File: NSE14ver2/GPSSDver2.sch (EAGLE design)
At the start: 30 parts, among them CN1 DM3AT, Q2 16mhz

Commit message: 修正
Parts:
- removed LED4, LED6: (no value), led:LED5MM
- added L1, L2: (no value), Chip LED:OSXX1608C1A
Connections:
- removed net N$12: C3.1, R16.2, SW1.P$2, U$3.PC6RESET
- new net RESETB: C3.1, JP1.6, R16.2, SW1.P$2, U$3.PC6RESET
- net +5V: now also R16.1
- net GND: now also L1.CT, L2.CT; no longer LED4.C, LED6.C, R16.1
- net N$1: now also L2.AN; no longer LED6.A
- net N$11: now also L1.AN; no longer LED4.A
- net SS: no longer JP1.6
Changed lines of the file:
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@@
 <setting verticaltext="up"/>
 </settings>
-<grid distance="0.1" unitdist="inch" unit="inch" style="lines" multiple="1" display="no" altdistance="0.01" altunitdist="inch" altunit="inch"/>
+<grid distance="0.05" unitdist="inch" unit="inch" style="lines" multiple="1" display="no" altdistance="0.01" altunitdist="inch" altunit="inch"/>
 <layers>
 <layer number="1" name="Top" color="4" fill="1" visible="no" active="no"/>
@@
 <part name="R4" library="rcl" library_urn="urn:adsk.eagle:library:334" deviceset="R-US_" device="R0603" package3d_urn="urn:adsk.eagle:package:23555/3" value="100"/>
 <part name="R13" library="rcl" library_urn="urn:adsk.eagle:library:334" deviceset="R-US_" device="R0603" package3d_urn="urn:adsk.eagle:package:23555/3" value="100"/>
-<part name="LED4" library="led" library_urn="urn:adsk.eagle:library:259" deviceset="LED" device="5MM" package3d_urn="urn:adsk.eagle:package:15799/2"/>
-<part name="LED6" library="led" library_urn="urn:adsk.eagle:library:259" deviceset="LED" device="5MM" package3d_urn="urn:adsk.eagle:package:15799/2"/>
 <part name="BMX2" library="BMX055" library_urn="urn:adsk.eagle:library:38466640" deviceset="BMX055" device="" package3d_urn="urn:adsk.eagle:package:38466643/2"/>
 <part name="P+7" library="supply1" library_urn="urn:adsk.eagle:library:371" deviceset="+5V" device=""/>
@@
 <part name="GND12" library="supply1" library_urn="urn:adsk.eagle:library:371" deviceset="GND" device=""/>
 <part name="GND13" library="supply1" library_urn="urn:adsk.eagle:library:371" deviceset="GND" device=""/>
-<part name="GND14" library="supply1" library_urn="urn:adsk.eagle:library:371" deviceset="GND" device=""/>
 <part name="GND15" library="supply1" library_urn="urn:adsk.eagle:library:371" deviceset="GND" device=""/>
 <part name="SW1" library="Tact switch" library_urn="urn:adsk.eagle:library:40248844" deviceset="TVAF06-A020B-R" device="" package3d_urn="urn:adsk.eagle:package:40248847/4"/>
@@
 <part name="P+1" library="supply1" library_urn="urn:adsk.eagle:library:371" deviceset="+5V" device=""/>
 <part name="GND1" library="supply1" library_urn="urn:adsk.eagle:library:371" deviceset="GND" device=""/>
+<part name="P+4" library="supply1" library_urn="urn:adsk.eagle:library:371" deviceset="+5V" device=""/>
+<part name="L1" library="Chip LED" library_urn="urn:adsk.eagle:library:38473657" deviceset="OSXX1608C1A" device="" package3d_urn="urn:adsk.eagle:package:38473660/2"/>
+<part name="L2" library="Chip LED" library_urn="urn:adsk.eagle:library:38473657" deviceset="OSXX1608C1A" device="" package3d_urn="urn:adsk.eagle:package:38473660/2"/>
 </parts>
 <sheets>
@@
 <attribute name="VALUE" x="207.772" y="88.9" size="1.778" layer="96" rot="R90"/>
 </instance>
-<instance part="LED4" gate="G$1" x="212.09" y="80.01" smashed="yes">
-<attribute name="NAME" x="215.646" y="75.438" size="1.778" layer="95" rot="R90"/>
-<attribute name="VALUE" x="217.805" y="75.438" size="1.778" layer="96" rot="R90"/>
-</instance>
-<instance part="LED6" gate="G$1" x="204.47" y="80.01" smashed="yes">
-<attribute name="NAME" x="208.026" y="75.438" size="1.778" layer="95" rot="R90"/>
-<attribute name="VALUE" x="210.185" y="75.438" size="1.778" layer="96" rot="R90"/>
-</instance>
 <instance part="BMX2" gate="G$1" x="227.33" y="176.53" smashed="yes">
 <attribute name="NAME" x="221.25" y="182.61" size="1.778" layer="95"/>
@@
 <attribute name="VALUE" x="78.74" y="78.74" size="1.778" layer="96"/>
 </instance>
-<instance part="GND14" gate="1" x="45.72" y="68.58" smashed="yes">
-<attribute name="VALUE" x="43.18" y="66.04" size="1.778" layer="96"/>
-</instance>
 <instance part="GND15" gate="1" x="116.84" y="81.28" smashed="yes">
 <attribute name="VALUE" x="114.3" y="78.74" size="1.778" layer="96"/>
@@
 <instance part="GND1" gate="1" x="233.68" y="60.96" smashed="yes">
 <attribute name="VALUE" x="231.14" y="58.42" size="1.778" layer="96"/>
+</instance>
+<instance part="P+4" gate="1" x="45.72" y="68.58" smashed="yes" rot="R180">
+<attribute name="VALUE" x="48.26" y="73.66" size="1.778" layer="96" rot="R270"/>
+</instance>
+<instance part="L1" gate="G$1" x="212.09" y="78.74" smashed="yes" rot="R270">
+<attribute name="NAME" x="209.042" y="81.788" size="1.27" layer="95" rot="R270"/>
+<attribute name="VALUE" x="214.63" y="84.074" size="1.27" layer="96" rot="R270"/>
+</instance>
+<instance part="L2" gate="G$1" x="204.47" y="78.74" smashed="yes" rot="R270">
+<attribute name="NAME" x="201.422" y="81.788" size="1.27" layer="95" rot="R270"/>
+<attribute name="VALUE" x="207.01" y="84.074" size="1.27" layer="96" rot="R270"/>
 </instance>
 </instances>
@@
 <wire x1="233.68" y1="73.66" x2="228.6" y2="73.66" width="0.1524" layer="91"/>
 <wire x1="228.6" y1="73.66" x2="228.6" y2="63.5" width="0.1524" layer="91"/>
+</segment>
+<segment>
+<pinref part="R16" gate="G$1" pin="1"/>
+<wire x1="45.72" y1="73.66" x2="45.72" y2="71.12" width="0.1524" layer="91"/>
+<pinref part="P+4" gate="1" pin="+5V"/>
 </segment>
 </net>
@@
 <junction x="212.09" y="72.39"/>
 <pinref part="GND26" gate="1" pin="GND"/>
-<pinref part="LED4" gate="G$1" pin="C"/>
-<wire x1="212.09" y1="74.93" x2="212.09" y2="72.39" width="0.1524" layer="91"/>
-<pinref part="LED6" gate="G$1" pin="C"/>
-<wire x1="204.47" y1="74.93" x2="204.47" y2="72.39" width="0.1524" layer="91"/>
+<wire x1="212.09" y1="76.2" x2="212.09" y2="72.39" width="0.1524" layer="91"/>
+<wire x1="204.47" y1="76.2" x2="204.47" y2="72.39" width="0.1524" layer="91"/>
+<pinref part="L2" gate="G$1" pin="CT"/>
+<pinref part="L1" gate="G$1" pin="CT"/>
 </segment>
 <segment>
@@
 <wire x1="81.28" y1="101.6" x2="81.28" y2="83.82" width="0.1524" layer="91"/>
 <pinref part="GND13" gate="1" pin="GND"/>
-</segment>
-<segment>
-<pinref part="R16" gate="G$1" pin="1"/>
-<wire x1="45.72" y1="73.66" x2="45.72" y2="71.12" width="0.1524" layer="91"/>
-<pinref part="GND14" gate="1" pin="GND"/>
 </segment>
 <segment>
@@
 <segment>
 <pinref part="R13" gate="G$1" pin="1"/>
-<pinref part="LED6" gate="G$1" pin="A"/>
-<wire x1="204.47" y1="87.63" x2="204.47" y2="82.55" width="0.1524" layer="91"/>
+<wire x1="204.47" y1="87.63" x2="204.47" y2="81.28" width="0.1524" layer="91"/>
+<pinref part="L2" gate="G$1" pin="AN"/>
 </segment>
 </net>
@@
 <segment>
 <pinref part="R4" gate="G$1" pin="1"/>
-<pinref part="LED4" gate="G$1" pin="A"/>
-<wire x1="212.09" y1="87.63" x2="212.09" y2="82.55" width="0.1524" layer="91"/>
+<wire x1="212.09" y1="87.63" x2="212.09" y2="81.28" width="0.1524" layer="91"/>
+<pinref part="L1" gate="G$1" pin="AN"/>
 </segment>
 </net>
@@
 </segment>
 </net>
-<net name="N$12" class="0">
+<net name="RESETB" class="0">
 <segment>
 <pinref part="U$3" gate="G$1" pin="PC6RESET"/>
@@
 <wire x1="45.72" y1="88.9" x2="35.56" y2="88.9" width="0.1524" layer="91"/>
 <junction x="45.72" y="88.9"/>
+<wire x1="45.72" y1="83.82" x2="53.34" y2="83.82" width="0.1524" layer="91"/>
+<wire x1="53.34" y1="83.82" x2="53.34" y2="78.74" width="0.1524" layer="91"/>
+<label x="53.34" y="78.74" size="1.778" layer="95" rot="R270" xref="yes"/>
+</segment>
+<segment>
+<pinref part="JP1" gate="A" pin="6"/>
+<wire x1="245.11" y1="140.97" x2="245.11" y2="133.35" width="0.1524" layer="91"/>
+<label x="245.11" y="133.35" size="1.778" layer="95" rot="R270" xref="yes"/>
 </segment>
 </net>
@@
 </segment>
 <segment>
-<pinref part="JP1" gate="A" pin="6"/>
-<wire x1="245.11" y1="140.97" x2="245.11" y2="133.35" width="0.1524" layer="91"/>
-<label x="245.11" y="133.35" size="1.778" layer="95" rot="R270" xref="yes"/>
-</segment>
-<segment>

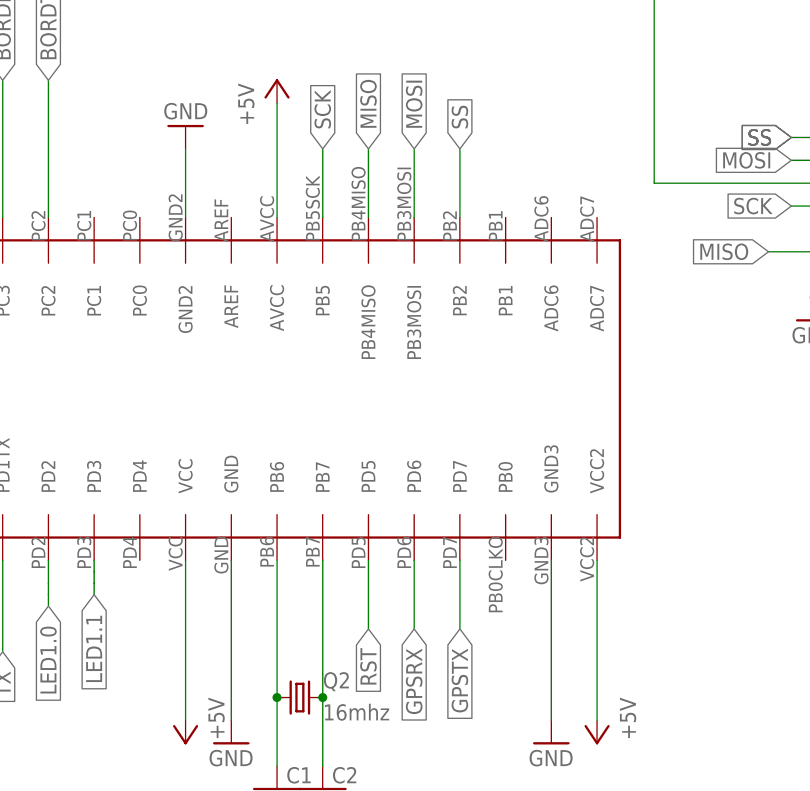
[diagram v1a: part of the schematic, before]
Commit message: 328修正
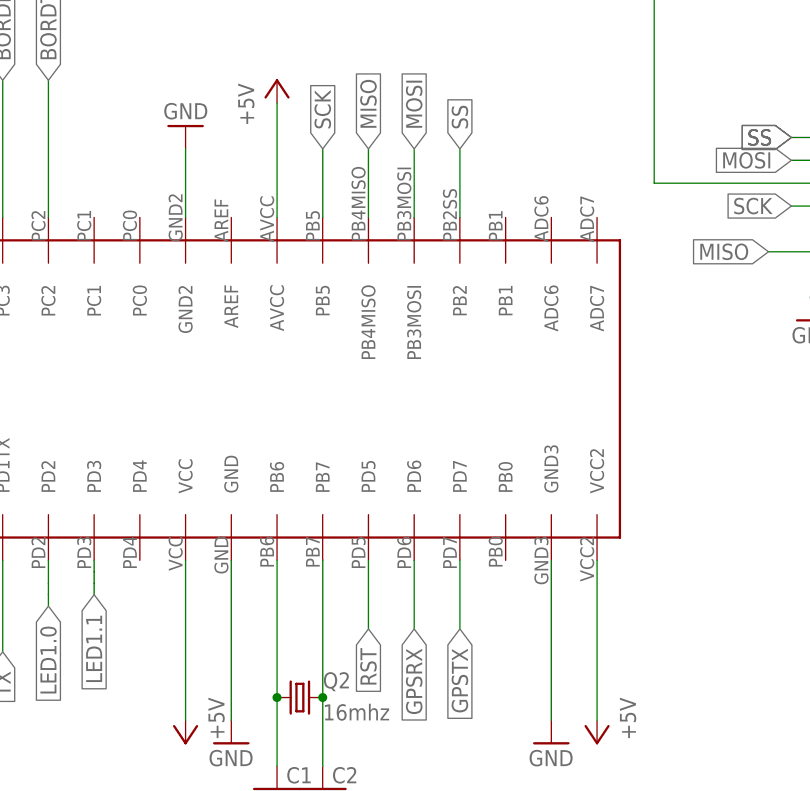
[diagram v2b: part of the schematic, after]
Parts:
- U$3: device ATmega328p-PU:ATMEGA328P-AU -> ATMAGA328P-AU:ATMEGA328P-AU
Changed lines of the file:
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@@
 <setting verticaltext="up"/>
 </settings>
-<grid distance="0.05" unitdist="inch" unit="inch" style="lines" multiple="1" display="no" altdistance="0.01" altunitdist="inch" altunit="inch"/>
+<grid distance="0.1" unitdist="inch" unit="inch" style="lines" multiple="1" display="no" altdistance="0.01" altunitdist="inch" altunit="inch"/>
 <layers>
 <layer number="1" name="Top" color="4" fill="1" visible="no" active="no"/>
@@
 <part name="P+7" library="supply1" library_urn="urn:adsk.eagle:library:371" deviceset="+5V" device=""/>
 <part name="GND10" library="supply1" library_urn="urn:adsk.eagle:library:371" deviceset="GND" device=""/>
-<part name="U$3" library="ATmega328p-PU" deviceset="ATMEGA328P-AU" device="" package3d_urn="urn:adsk.eagle:package:44716433/1"/>
+<part name="U$3" library="ATMAGA328P-AU" deviceset="ATMEGA328P-AU" device="" package3d_urn="urn:adsk.eagle:package:44744060/1"/>
 <part name="R16" library="rcl" library_urn="urn:adsk.eagle:library:334" deviceset="R-US_" device="R0603" package3d_urn="urn:adsk.eagle:package:23555/3" value="10k"/>
 <part name="Q2" library="crystal" library_urn="urn:adsk.eagle:library:204" deviceset="CRYSTAL" device="HC49UP" package3d_urn="urn:adsk.eagle:package:12078/1" value="16mhz"/>
